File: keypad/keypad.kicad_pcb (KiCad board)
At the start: 2 copper layers, 70 x 100 mm, 14 parts, among them J1 Conn_01x01, J10 Conn_01x01, J11 Conn_01x01, J12 Conn_01x01, J13 Conn_01x16, J2 Conn_01x01, J3 Conn_01x01, J4 Conn_01x01, J5 Conn_01x01, J6 Conn_01x01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

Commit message: keypad rev 1 done + gerber
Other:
- board text added: "JLCJLCJLCJLC"
- board text added: "clue & dj505 | https://github.com/dj505/low-key-amuse"
- board text added: "low-key-amuse prototype rev. 1"

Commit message: Alignment fixes, generate gerbers
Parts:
- added G***: LOGO, LogoFootprints:Arrow_6, B.Cu at (172.5, 55.6)
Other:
- board text added: "https://github.com/dj505/low-key-amuse"
- board text added: "low-key-amuse | clue & dj505"
- board text removed: "clue & dj505 | https://github.com/dj505/low-key-amuse"
- board text removed: "low-key-amuse prototype rev. 1"

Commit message: Add tooling holes, update logo, other adjustments
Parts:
- removed the G*** at (172.5, 55.6)
- added G***: LOGO, low-key-amuse:logo_large, B.Cu at (142.4, 98.2)
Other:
- board text added: "by clue & dj505"
- board text added: "github.com/dj505/low-key-amuse"
- board text removed: "https://github.com/dj505/low-key-amuse"
- board text removed: "low-key-amuse | clue & dj505"

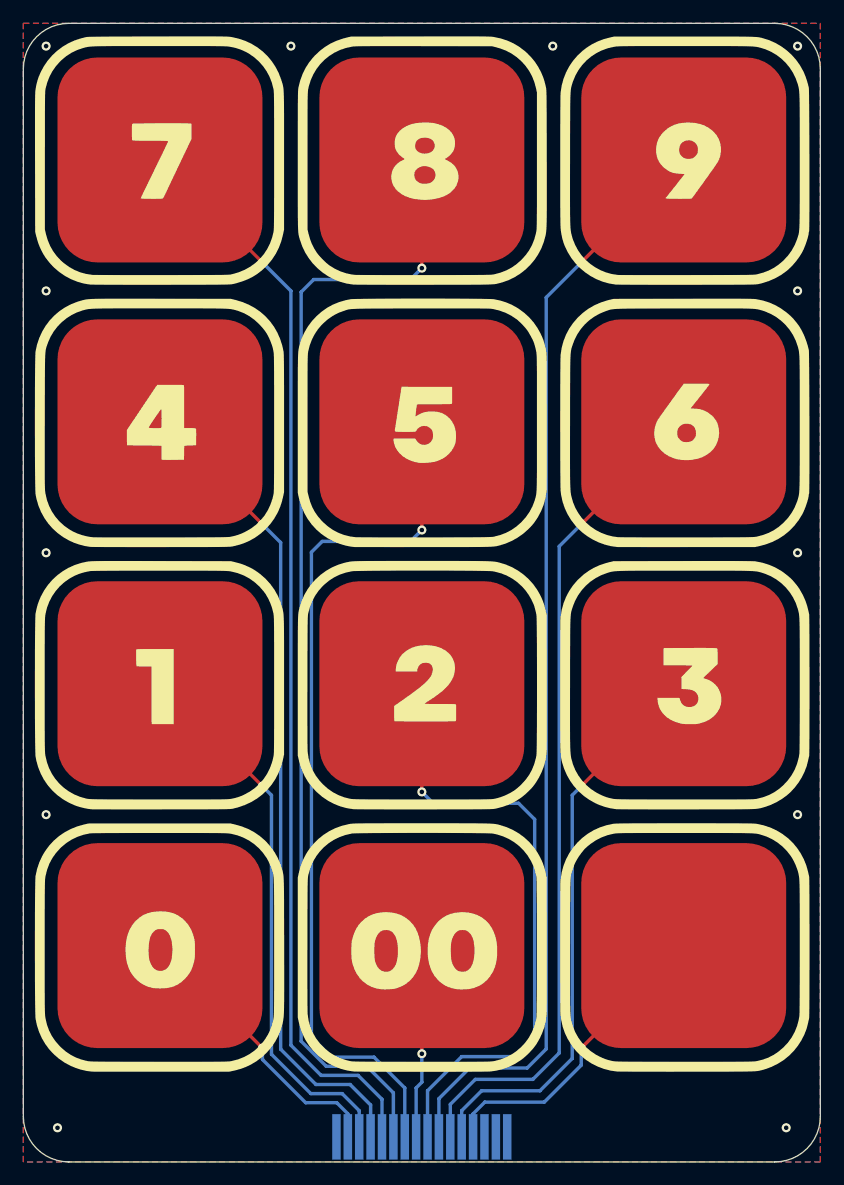
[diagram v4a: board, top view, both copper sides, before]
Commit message: Update keypad with ffc connector
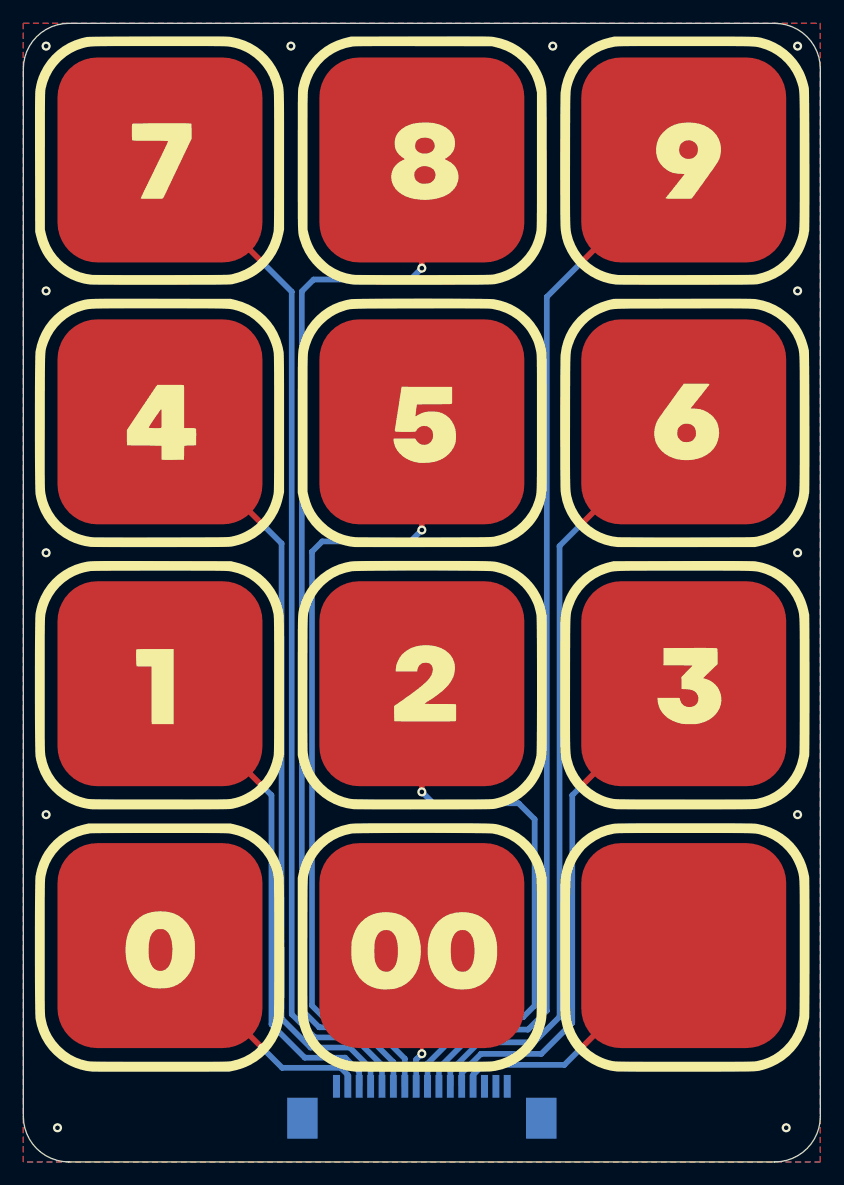
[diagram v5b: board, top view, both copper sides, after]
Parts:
- J13: footprint Edge Connector:1.0mm Pitch Edge Connector 01x16 -> Connector_FFC-FPC:TE_1-84952-6_1x16-1MP_P1.0mm_Horizontal
- moved J13 2.64 mm to (143.0, 145.2)
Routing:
- net Net-(J13-Pin_8): track 55.3 -> 50.3 mm
- net Net-(J13-Pin_7): track 97.7 -> 92.9 mm
- net Net-(J13-Pin_10): track 77.0 -> 72.3 mm
- net Net-(J10-Pin_1): track 74.3 -> 69.7 mm
- net Net-(J13-Pin_11): track 100.6 -> 96.1 mm
- net Net-(J13-Pin_9): track 17.0 -> 12.6 mm
- net Net-(J11-Pin_1): track 50.9 -> 46.5 mm
- net Net-(J1-Pin_1): track 95.8 -> 91.5 mm
- net Net-(J13-Pin_13): track 72.2 -> 68.0 mm
- net Net-(J13-Pin_14): track 48.7 -> 44.7 mm
- net Net-(J12-Pin_1): track 27.5 -> 24.2 mm
- net Net-(J13-Pin_15): track 25.2 -> 22.2 mm
